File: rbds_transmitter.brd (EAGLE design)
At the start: 160 x 100 mm, 136 parts, among them J2 AVRISP-6, Q1 P-CH, Q2 P-Ch, Q3 P-Ch, T1 ATB3225-75034CT, T2 ATB3225-75034CT, U1 MAX2606, U2 TS974, U3 TS974, U4 MAX1551, U5 ATMEGA328, U6 TPS61030, U7 MCP4812, X1 16Mhz

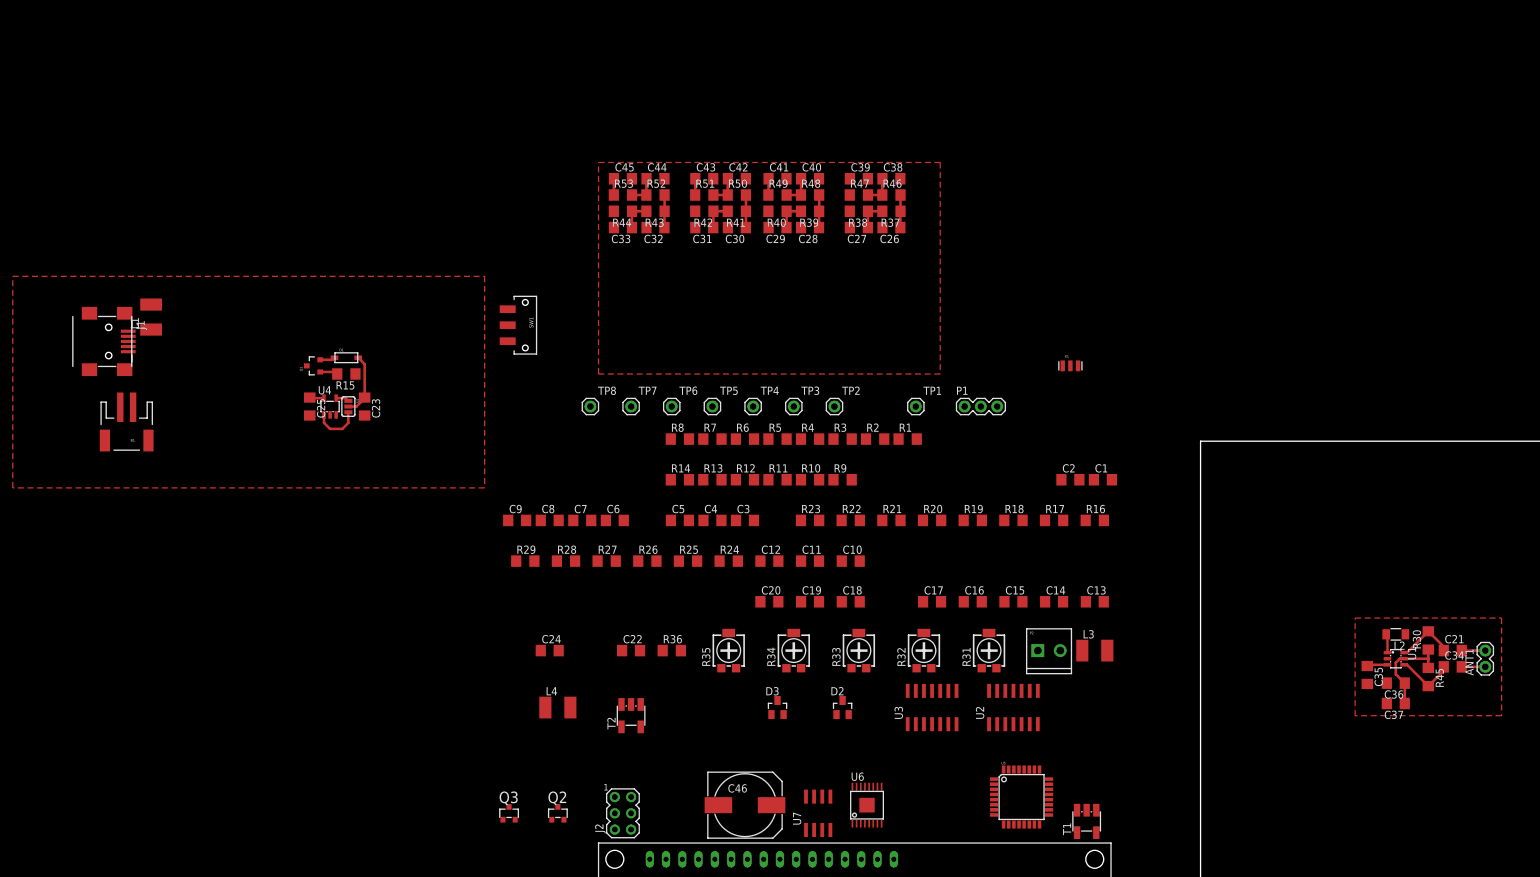
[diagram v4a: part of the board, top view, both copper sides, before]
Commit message: schematic update: corrected 5v connection
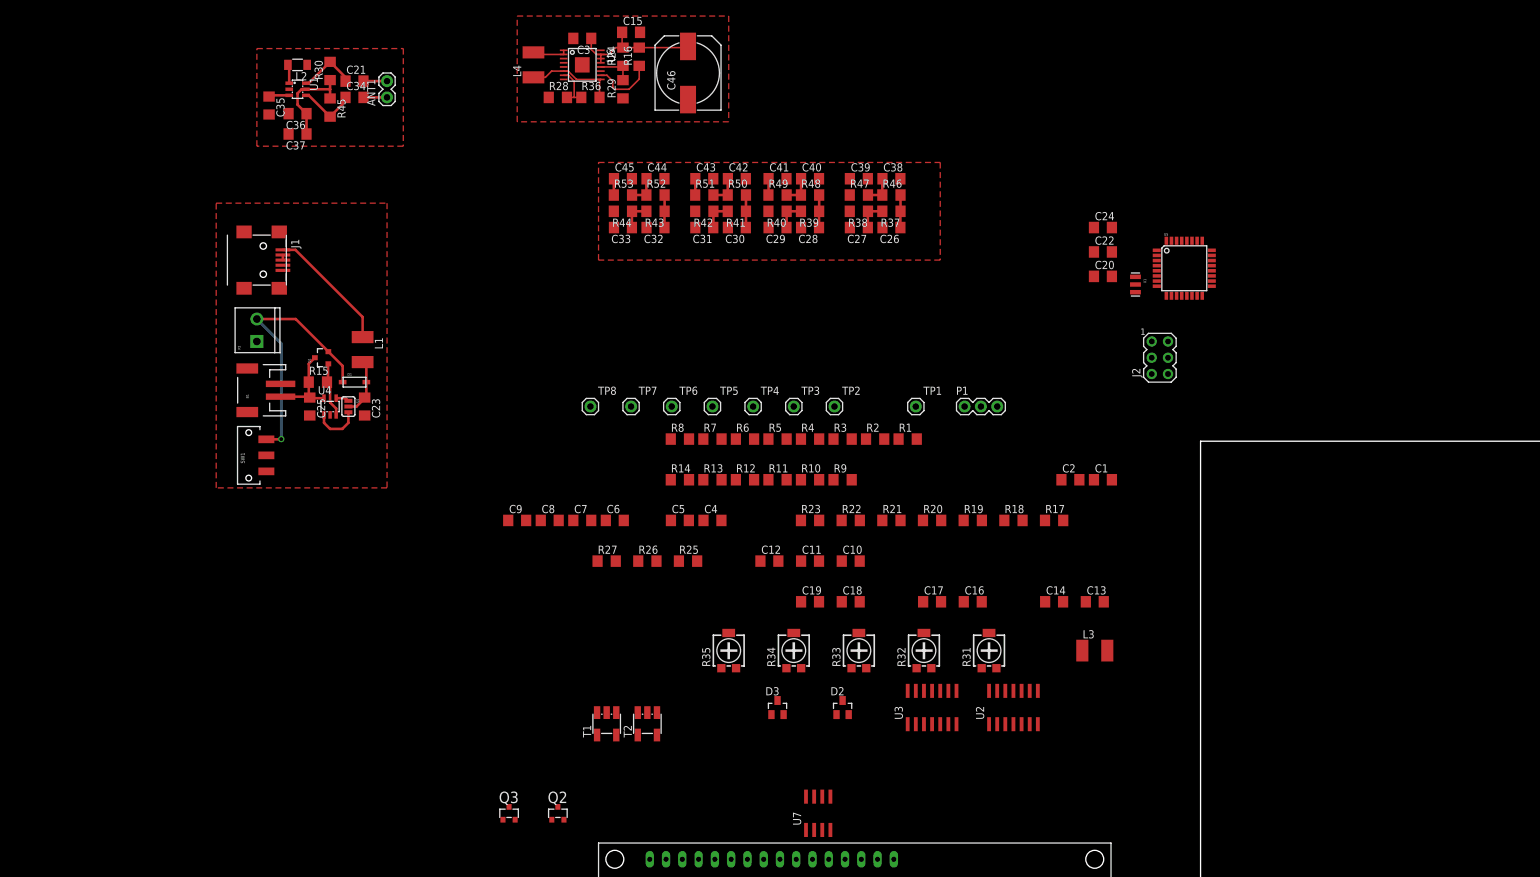
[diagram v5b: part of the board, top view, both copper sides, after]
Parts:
- moved R30 193.1 mm to (-135.9, 157.8)
- moved C21 193.1 mm to (-132.1, 156.2)
- moved C34 193.1 mm to (-132.1, 153.7)
- moved ANT1 193.1 mm to (-127.0, 153.7)
- moved C35 193.1 mm to (-145.4, 152.4)
- moved C36 193.1 mm to (-141.0, 151.1)
- moved C37 193.1 mm to (-141.0, 148.0)
- moved L2 193.1 mm to (-141.0, 158.8)
- moved R45 193.1 mm to (-135.9, 152.1)
- moved U1 193.1 mm to (-141.0, 154.9)
- moved P2 131.1 mm to (-147.3, 115.6), turned to 90 degrees
- moved U6 123.8 mm to (-96.5, 158.8), turned to 270 degrees
- moved C46 114.6 mm to (-80.0, 157.5), turned to 90 degrees
- moved J2 109.9 mm to (-6.35, 113.0)
- moved C24 108.7 mm to (-15.2, 133.3)
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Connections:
- removed net N$6: D1.C, Q1.2, SW1.3
- new net N$15: D1.C, P2.2, Q1.2, SW1.3
- net +5V: no longer P2.2
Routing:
- net N$15: track 0.00 -> 41.6 mm, vias 0 -> 1
- net +5V: track 0.00 -> 21.7 mm
- net N$54: track 0.00 -> 20.6 mm
- net N$50: track 0.00 -> 14.4 mm
- net N$11: track 2.27 -> 13.6 mm
- net LOWBAT: track 0.00 -> 10.2 mm
- net U7: track 0.00 -> 6.79 mm
- net N$10: track 2.79 -> 9.00 mm
- net N$17: track 0.00 -> 5.76 mm
- net N$12: track 0.00 -> 5.50 mm
- net N$6: track 2.36 -> 0.00 mm
- net N$13: track 0.00 -> 0.80 mm

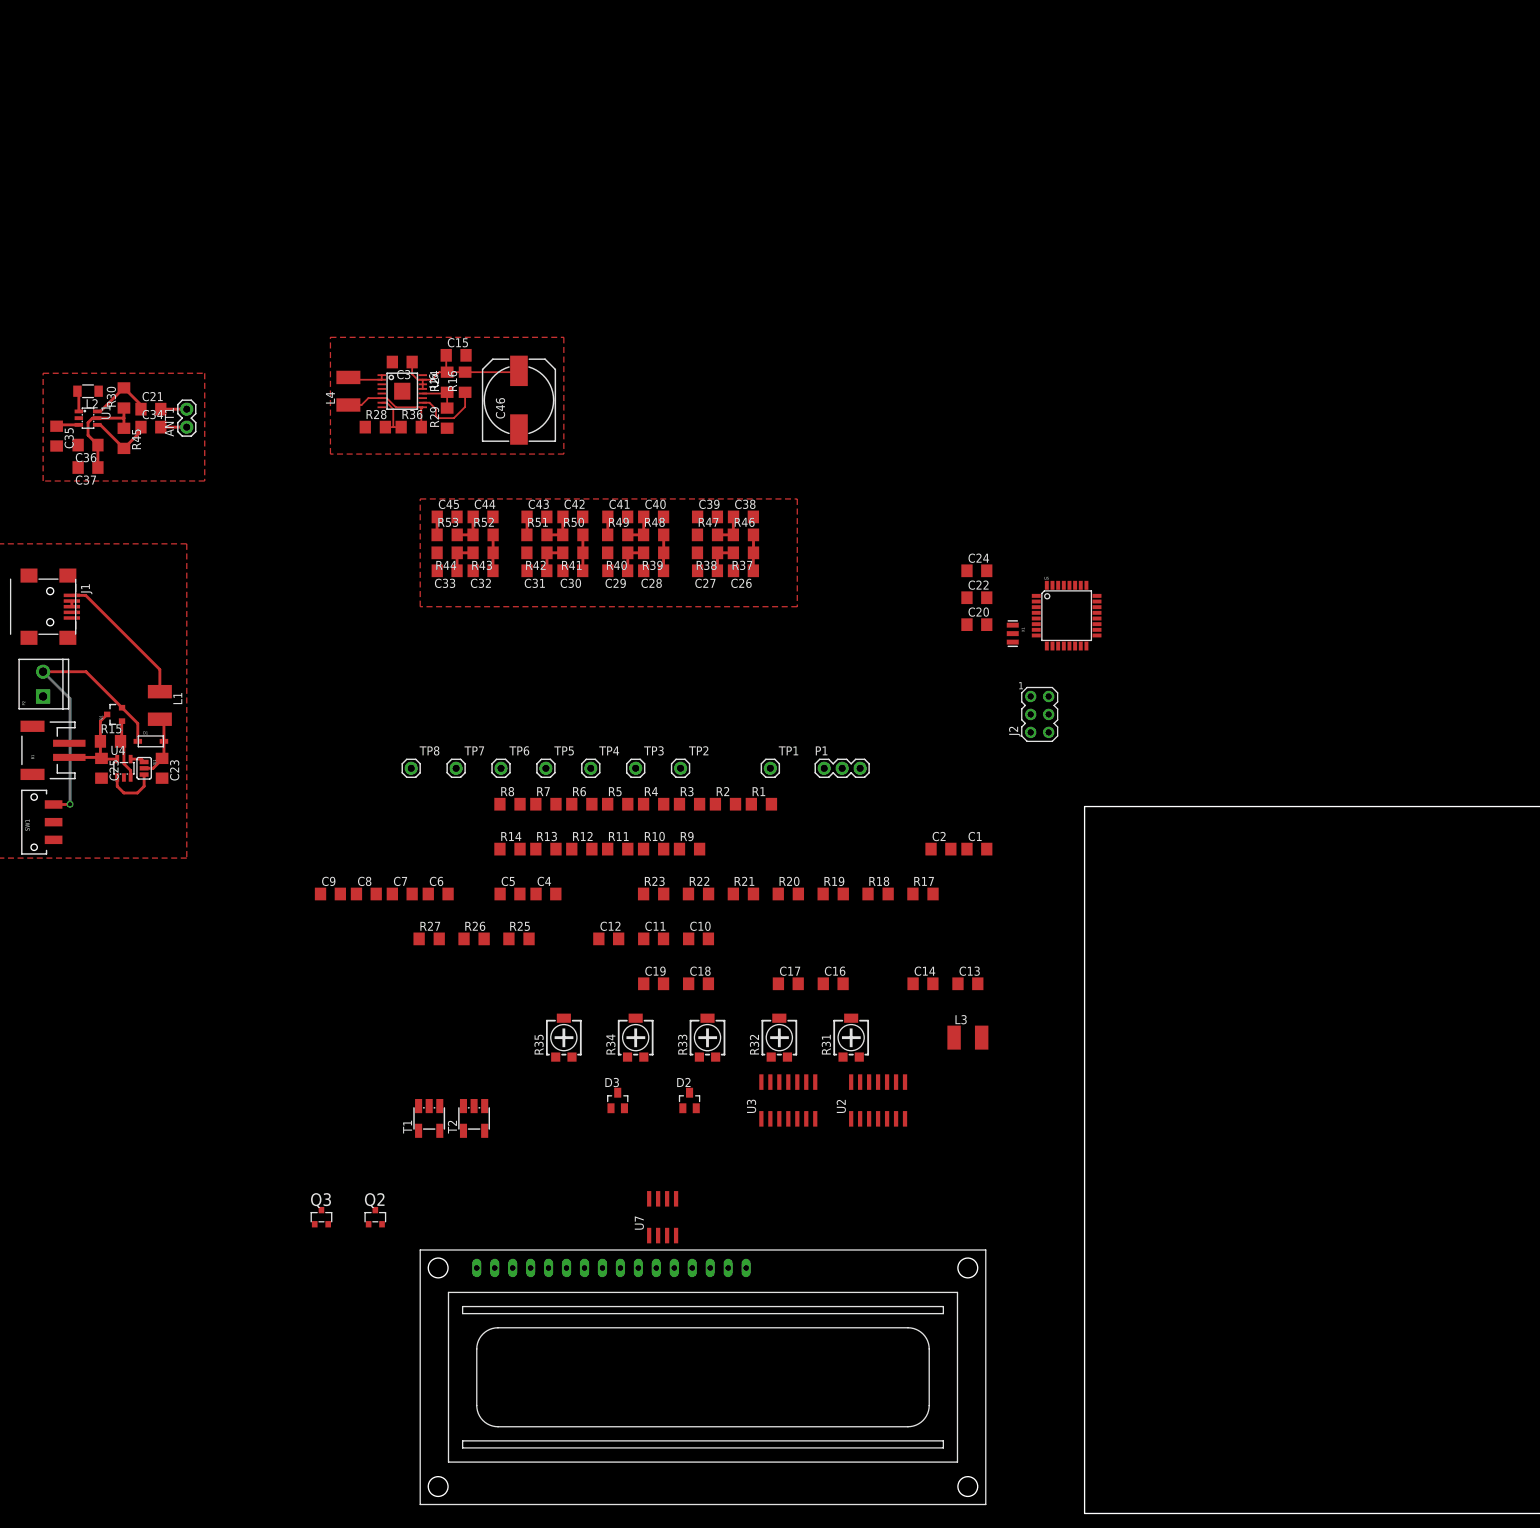
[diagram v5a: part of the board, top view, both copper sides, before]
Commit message: changed transformer layout
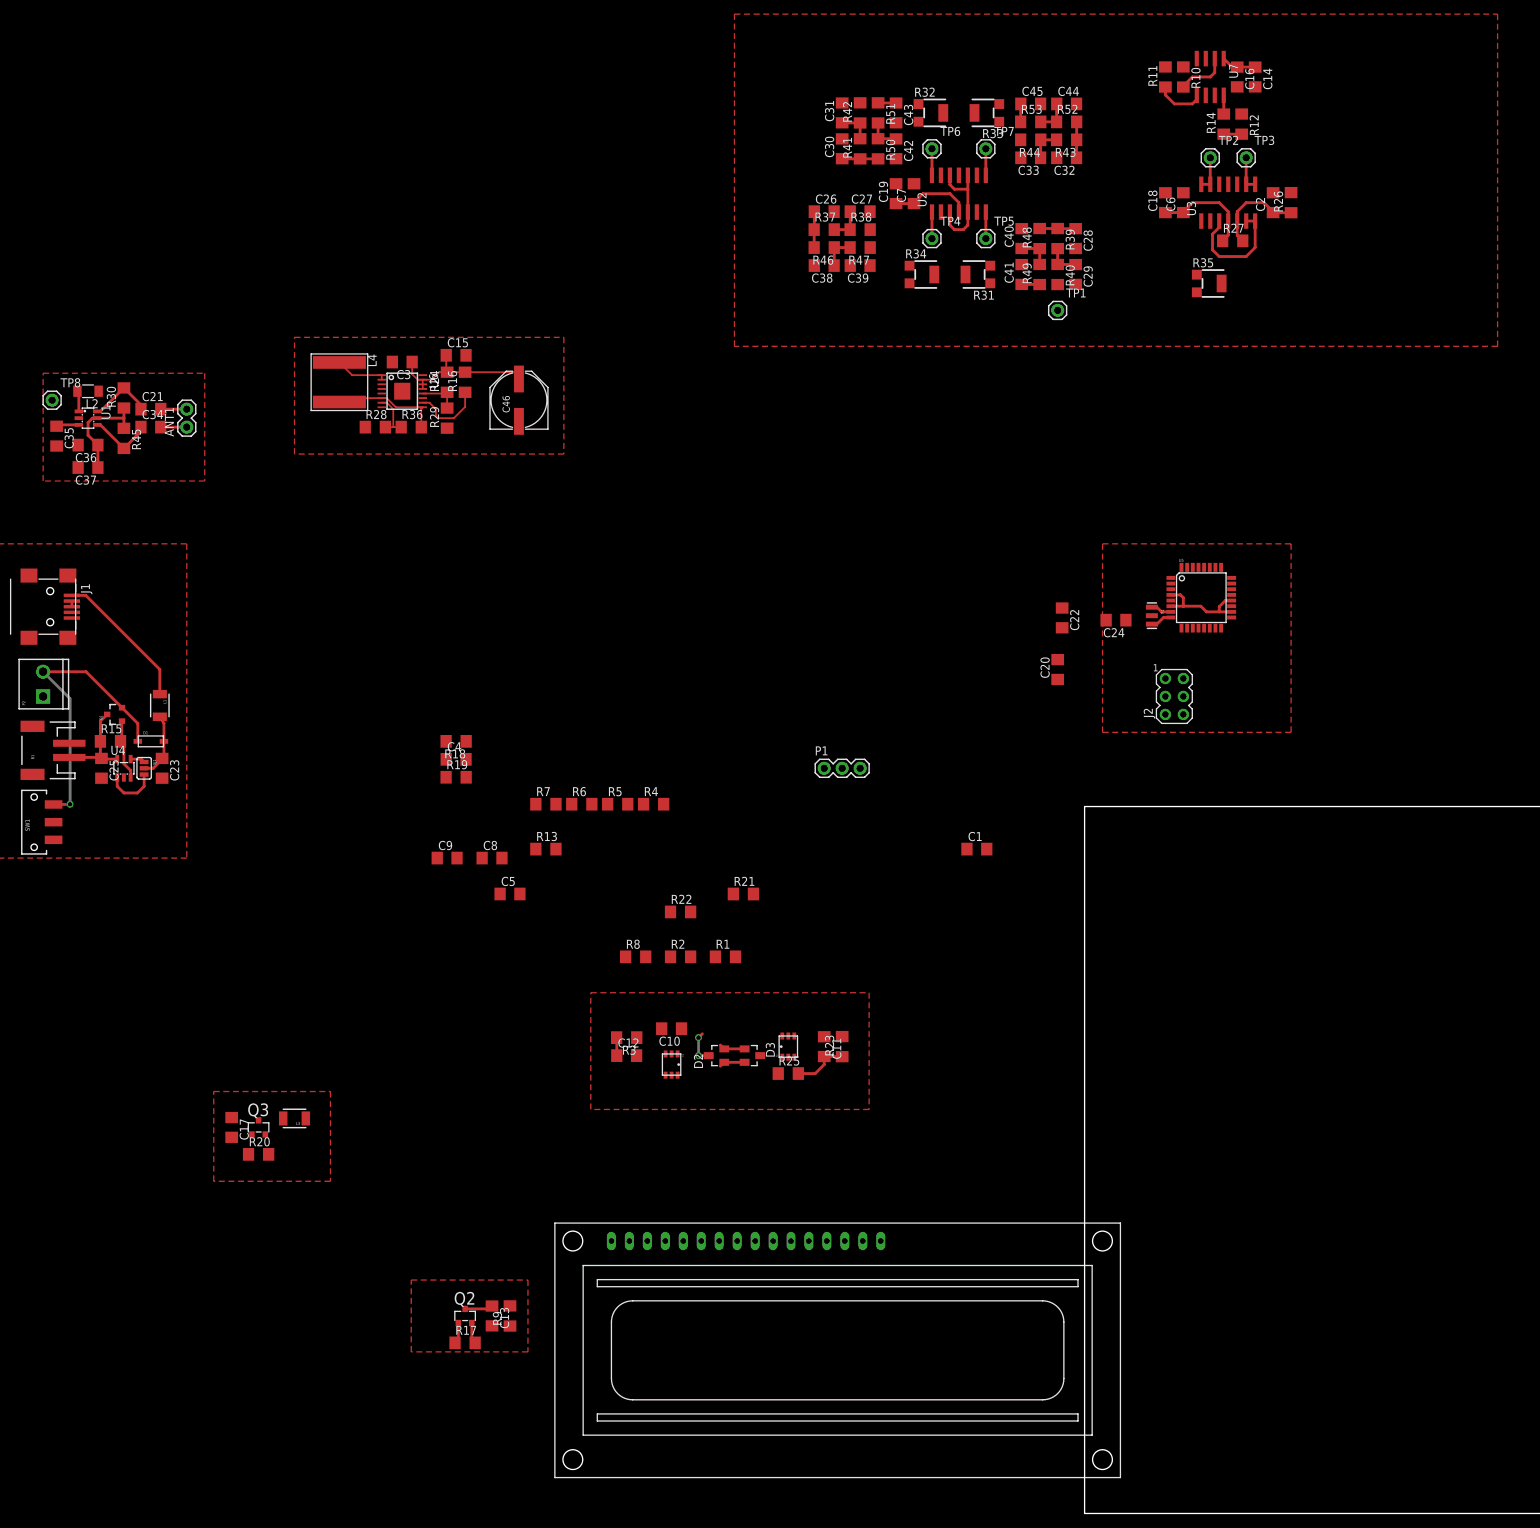
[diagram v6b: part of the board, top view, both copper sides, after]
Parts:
- C46: device adafruit:140CLH-1014 -> adafruit:PANASONIC_E
- L1, L3: device resistor:L1812 -> sparkfun:1210
- L4: device rcl:L1812 -> yuden:8040
- R31, R32, R33, R34, R35: device rcl:RTRIM4G/J -> rcl:RTRIM3304W
- T1, T2: value ATB3225-75034CT -> ATB3225-75032CT; device inductor-neosid:SM-T4 -> tdk:TRANS
- moved U7 178.9 mm to (17.8, 203.2), turned to 180 degrees
- moved R26 155.6 mm to (29.2, 185.4), turned to 90 degrees
- moved R27 150.6 mm to (21.0, 180.0)
- moved R14 143.9 mm to (19.7, 196.5), turned to 90 degrees
- moved C6 143.8 mm to (14.0, 185.4), turned to 90 degrees
- moved U3 141.4 mm to (20.3, 185.4)
- moved R35 140.5 mm to (17.8, 174.0), turned to 270 degrees
- moved C16 140.4 mm to (21.6, 203.2), turned to 270 degrees
- moved R12 138.7 mm to (22.2, 196.5), turned to 270 degrees
- moved R33 136.6 mm to (-14.0, 198.1), turned to 90 degrees
- moved C14 136.6 mm to (24.1, 203.2), turned to 270 degrees
- moved R11 133.9 mm to (11.4, 203.2), turned to 90 degrees
- moved R32 132.6 mm to (-21.6, 198.1), turned to 270 degrees
- moved R10 132.5 mm to (14.0, 203.2), turned to 270 degrees
- moved U2 128.8 mm to (-17.8, 186.7)
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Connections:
- net +5V: no longer C46.+
- net GND: now also T1.6, T2.2, T2.5; no longer C46.-, T1.5, T2.3
- net N$12: now also L4.1; no longer L4.2
- net N$14: now also T2.3; no longer T2.2
- net N$16: now also T1.3; no longer T1.2
- net N$19: now also T1.2, T1.5; no longer T1.3
- net N$42: now also T2.6; no longer T2.5
- net N$50: now also L4.2; no longer L4.1
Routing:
- net AGND: track 0.00 -> 32.5 mm
- net VCC: track 15.1 -> 46.0 mm
- net +5V: track 21.7 -> 39.6 mm
- net N$66: track 0.00 -> 13.3 mm
- net RBDS: track 0.00 -> 7.87 mm
- net !DAC_CS: track 0.00 -> 7.35 mm
- net !DAC_LATCH: track 0.00 -> 6.93 mm
- net FREQUENCY: track 0.00 -> 5.02 mm
- net BPSK: track 0.00 -> 5.02 mm
- net N$3: track 0.00 -> 4.75 mm, vias 0 -> 2
- net VDD: track 0.00 -> 3.98 mm
- net N$71: track 0.00 -> 3.81 mm
- net N$82: track 0.00 -> 3.75 mm
- net N$76: track 0.00 -> 3.75 mm
- net N$65: track 0.00 -> 3.75 mm
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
